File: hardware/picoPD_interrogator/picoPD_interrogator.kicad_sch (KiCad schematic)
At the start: 53 parts, among them J1 Conn_01x07, J2 USB_C_Receptacle_USB2.0_16P, J3 Conn_01x14, Q1 rohm-RE1C002UN, Q2 rohm-RE1C002UN, Q3 rohm-RE1C002UN, Q4 rohm-RE1C002UN, Q5 rohm-RE1C002UN, SW1 RESET_BTN, U3 ST-LM393QT, U6 LV2862XDDC

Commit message: PCB: Working on PCB layout.
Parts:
- TP1: footprint TestPoint:TestPoint_Pad_D4.0mm -> TestPoint:TestPoint_Pad_D2.5mm
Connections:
- net USB_DM_CONN: now reaches J2.A7 (D-), J2.B7 (D-), R27.2
- net USB_DP_CONN: now reaches J2.A6 (D+), J2.B6 (D+), R28.2
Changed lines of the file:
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@@
 		)
 	)
+	(label "USB_DP_CONN"
+		(at 264.16 57.15 180)
+		(effects
+			(font
+				(size 1.27 1.27)
+			)
+			(justify right)
+		)
+	)
 	(label "CC2_TX_L"
 		(at 133.35 63.5 180)
@@
 		)
 	)
+	(label "USB_DM_CONN"
+		(at 264.16 52.07 180)
+		(effects
+			(font
+				(size 1.27 1.27)
+			)
+			(justify right)
+		)
+	)
 	(label "SCL"
 		(at 36.83 99.06 0)
@@
 			)
 		)
-		(property "Footprint" "TestPoint:TestPoint_Pad_D4.0mm"
+		(property "Footprint" "TestPoint:TestPoint_Pad_D2.5mm"
 			(at 156.21 179.07 0)
 			(effects

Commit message: PCB: Working on board layout.
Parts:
- added R29: 3.3K, Resistor_SMD:R_0201_0603Metric, symbol Device:R
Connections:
- net 3V3: now also R29.2
- net TCPC_INT: now also R29.1
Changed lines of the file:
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@@
+	(wire
+		(pts
+			(xy 27.94 187.96) (xy 27.94 185.42)
+		)
+		(stroke
+			(width 0)
+			(type default)
+		)
+	)
 	(wire
 		(pts
@@
 	(wire
 		(pts
+			(xy 25.4 187.96) (xy 27.94 187.96)
+		)
+		(stroke
+			(width 0)
+			(type default)
+		)
+	)
+	(wire
+		(pts
+			(xy 27.94 177.8) (xy 27.94 175.26)
+		)
+		(stroke
+			(width 0)
+			(type default)
+		)
+	)
+	(wire
+		(pts
 			(xy 34.29 128.27) (xy 33.02 128.27)
 		)
@@
 		(pts
 			(xy 264.16 111.76) (xy 270.51 111.76)
+		)
+		(stroke
+			(width 0)
+			(type default)
+		)
+	)
+	(wire
+		(pts
+			(xy 27.94 175.26) (xy 35.56 175.26)
 		)
 		(stroke
@@
 	)
 	(label "TCPC_INT"
-		(at 35.56 175.26 180)
+		(at 33.02 175.26 180)
 		(effects
 			(font
@@
 			)
 			(justify left)
+		)
+	)
+	(label "3V3"
+		(at 25.4 187.96 180)
+		(effects
+			(font
+				(size 1.27 1.27)
+			)
+			(justify right)
 		)
 	)
@@
 					(unit 1)
 				)
+			)
+		)
+	)
+	(symbol
+		(lib_id "Device:R")
+		(at 27.94 181.61 0)
+		(unit 1)
+		(exclude_from_sim no)
+		(in_bom yes)
+		(on_board yes)
+		(dnp no)
+		(property "Reference" "R29"
+			(at 25.908 181.61 90)
+			(effects
+				(font
+					(size 1.27 1.27)
+				)
+			)
+		)
+		(property "Value" "3.3K"
+			(at 27.94 181.61 90)
+			(effects
+				(font
+					(size 0.889 0.889)
+				)
+			)
+		)
+		(property "Footprint" "Resistor_SMD:R_0201_0603Metric"
+			(at 26.162 181.61 90)
+			(effects
+				(font
+					(size 1.27 1.27)
+				)
+				(hide yes)
+			)
+		)
+		(property "Datasheet" "~"
+			(at 27.94 181.61 0)
+			(effects
+				(font
+					(size 1.27 1.27)
+				)
+				(hide yes)
+			)
+		)
+		(property "Description" "Resistor"
+			(at 27.94 181.61 0)
+			(effects
+				(font
+					(size 1.27 1.27)
+				)
+				(hide yes)
+			)
+		)
+		(property "Manufacturer" "Panasonic Electronic Components"
+			(at 27.94 181.61 0)
+			(effects
+				(font
+					(size 1.27 1.27)
+				)
+				(hide yes)
+			)
+		)
+		(property "Description Detailed" "3.3 kOhms ±1% 0.05W, 1/20W Chip Resistor 0201 (0603 Metric) Thick Film"
+			(at 27.94 181.61 0)
+			(effects
+				(font
+					(size 1.27 1.27)
+				)
+				(hide yes)
+			)
+		)
+		(property "DigiKey PN" "P122937CT-ND"
+			(at 27.94 181.61 0)
+			(effects
+				(font
+					(size 1.27 1.27)
+				)
+				(hide yes)
+			)
+		)
+		(property "Manufacturer PN" "ERJ-1GNF3301C"
+			(at 27.94 181.61 0)
+			(effects
+				(font
+					(size 1.27 1.27)
+				)
+				(hide yes)
+			)
+		)
+		(pin "1"
+		)
+		(pin "2"
+		)
+		(instances
+			(project "picoPD_interrogator"
+				(path "/e34b0978-7def-4921-94d0-accc0a677529"
+					(reference "R29")
+					(unit 1)
+				)

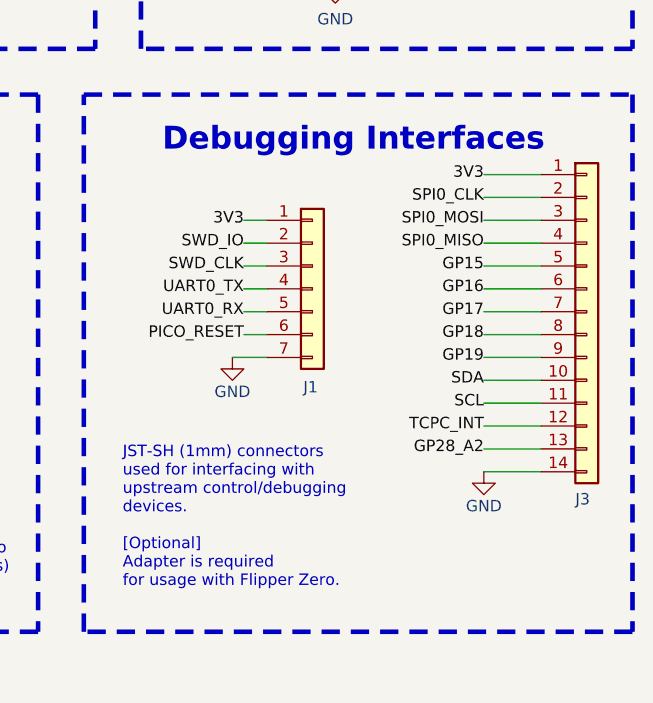
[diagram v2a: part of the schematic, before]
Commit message: PCB/Schematic: Added JST connector pins to the GND netlist.
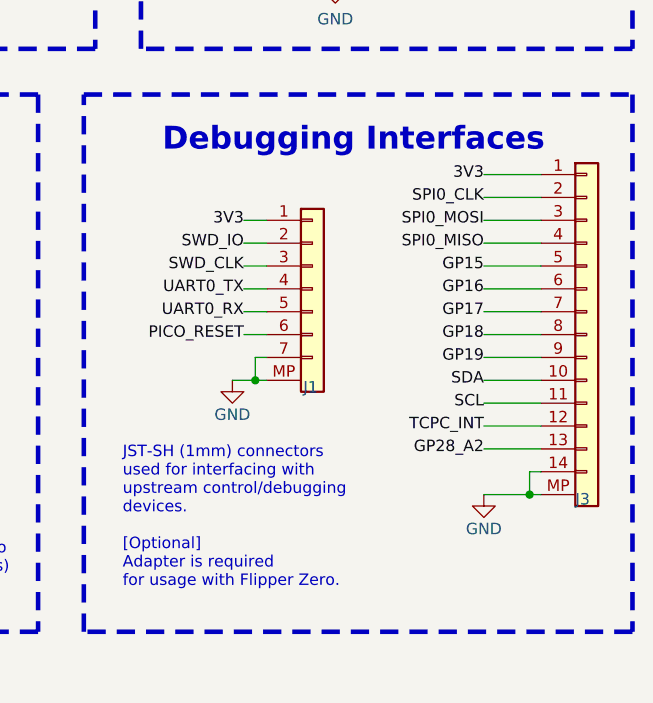
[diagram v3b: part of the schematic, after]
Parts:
- J1: symbol Connector_Generic:Conn_01x07 -> picoPD_interrogator:JST_7_pin
- J3: symbol Connector_Generic:Conn_01x14 -> picoPD_interrogator:JST_14_pin
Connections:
- net GND: now also J1.MP, J3.MP
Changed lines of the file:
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@@
 	)
 	(junction
+		(at 238.76 119.38)
+		(diameter 0)
+		(color 0 0 0 0)
+	)
+	(junction
 		(at 204.47 43.18)
 		(diameter 0)
@@
 	)
 	(junction
+		(at 269.24 132.08)
+		(diameter 0)
+		(color 0 0 0 0)
+	)
+	(junction
 		(at 143.51 116.84)
 		(diameter 0)
@@
 	(wire
 		(pts
-			(xy 264.16 129.54) (xy 270.51 129.54)
+			(xy 113.03 54.61) (xy 113.03 55.88)
 		)
 		(stroke
@@
 	(wire
 		(pts
-			(xy 113.03 54.61) (xy 113.03 55.88)
+			(xy 170.18 53.34) (xy 170.18 64.77)
 		)
 		(stroke
@@
 	(wire
 		(pts
-			(xy 170.18 53.34) (xy 170.18 64.77)
+			(xy 264.16 132.08) (xy 269.24 132.08)
 		)
 		(stroke
@@
 	(wire
 		(pts
-			(xy 236.22 116.84) (xy 240.03 116.84)
+			(xy 236.22 119.38) (xy 238.76 119.38)
 		)
 		(stroke
@@
 	(wire
 		(pts
+			(xy 240.03 116.84) (xy 238.76 116.84)
+		)
+		(stroke
+			(width 0)
+			(type default)
+		)
+	)
+	(wire
+		(pts
 			(xy 25.4 187.96) (xy 27.94 187.96)
 		)
@@
 	(wire
 		(pts
+			(xy 269.24 129.54) (xy 269.24 132.08)
+		)
+		(stroke
+			(width 0)
+			(type default)
+		)
+	)
+	(wire
+		(pts
 			(xy 95.25 116.84) (xy 95.25 118.11)
 		)
@@
 	(wire
 		(pts
+			(xy 238.76 119.38) (xy 240.03 119.38)
+		)
+		(stroke
+			(width 0)
+			(type default)
+		)
+	)
+	(wire
+		(pts
 			(xy 123.19 167.64) (xy 116.84 167.64)
 		)
@@
 	(wire
 		(pts
+			(xy 270.51 129.54) (xy 269.24 129.54)
+		)
+		(stroke
+			(width 0)
+			(type default)
+		)
+	)
+	(wire
+		(pts
 			(xy 203.2 55.88) (xy 203.2 59.69)
 		)
@@
 	(wire
 		(pts
+			(xy 238.76 116.84) (xy 238.76 119.38)
+		)
+		(stroke
+			(width 0)
+			(type default)
+		)
+	)
+	(wire
+		(pts
 			(xy 204.47 59.69) (xy 204.47 63.5)
 		)
@@
 	(wire
 		(pts
+			(xy 269.24 132.08) (xy 270.51 132.08)
+		)
+		(stroke
+			(width 0)
+			(type default)
+		)
+	)
+	(wire
+		(pts
 			(xy 91.44 106.68) (xy 95.25 106.68)
 		)
@@
 	(symbol
 		(lib_id "power:GND")
-		(at 236.22 116.84 0)
+		(at 236.22 119.38 0)
 		(unit 1)
 		(exclude_from_sim no)
@@
 		(dnp no)
 		(property "Reference" "#PWR023"
-			(at 236.22 123.19 0)
+			(at 236.22 125.73 0)
 			(effects
 				(font
@@
 		)
 		(property "Value" "GND"
-			(at 236.22 120.65 0)
+			(at 236.22 123.19 0)
 			(effects
 				(font
@@
 		)
 		(property "Footprint" ""
-			(at 236.22 116.84 0)
+			(at 236.22 119.38 0)
 			(effects
 				(font
@@
 		)
 		(property "Datasheet" ""
-			(at 236.22 116.84 0)
+			(at 236.22 119.38 0)
 			(effects
 				(font
@@
 		)
 		(property "Description" "Power symbol creates a global label with name \"GND\" , ground"
-			(at 236.22 116.84 0)
+			(at 236.22 119.38 0)
 			(effects
 				(font
@@
 	(symbol
 		(lib_id "power:GND")
-		(at 264.16 129.54 0)
+		(at 264.16 132.08 0)
 		(unit 1)
 		(exclude_from_sim no)
@@
 		(dnp no)
 		(property "Reference" "#PWR025"
-			(at 264.16 135.89 0)
+			(at 264.16 138.43 0)
 			(effects
 				(font
@@
 		)
 		(property "Value" "GND"
-			(at 264.16 133.35 0)
+			(at 264.16 135.89 0)
 			(effects
 				(font
@@
 		)
 		(property "Footprint" ""
-			(at 264.16 129.54 0)
+			(at 264.16 132.08 0)
 			(effects
 				(font
@@
 		)
 		(property "Datasheet" ""
-			(at 264.16 129.54 0)
+			(at 264.16 132.08 0)
 			(effects
 				(font
@@
 		)
 		(property "Description" "Power symbol creates a global label with name \"GND\" , ground"
-			(at 264.16 129.54 0)
+			(at 264.16 132.08 0)
 			(effects
 				(font
@@
 	)
 	(symbol
-		(lib_id "Connector_Generic:Conn_01x07")
+		(lib_id "picoPD_interrogator:JST_7_pin")
 		(at 245.11 109.22 0)
 		(unit 1)
@@
 		(pin "5"
 		)
+		(pin "MP"
+		)
 		(instances
 			(project ""
@@
 	)
 	(symbol
-		(lib_id "Connector_Generic:Conn_01x14")
+		(lib_id "picoPD_interrogator:JST_14_pin")
 		(at 275.59 111.76 0)
 		(unit 1)
@@
 		(pin "8"
 		)
+		(pin "MP"
+		)
 		(instances

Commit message: PCB: Working on PCB layout.
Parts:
- added C7: 1uF, Capacitor_SMD:C_0603_1608Metric, symbol Device:C
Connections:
- net 3V3: now also C7.2
- net GND: now also C7.1
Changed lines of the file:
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@@
 	)
 	(junction
+		(at 62.23 180.34)
+		(diameter 0)
+		(color 0 0 0 0)
+	)
+	(junction
 		(at 114.3 184.15)
 		(diameter 0)
@@
 	)
 	(junction
+		(at 57.15 172.72)
+		(diameter 0)
+		(color 0 0 0 0)
+	)
+	(junction
 		(at 143.51 116.84)
 		(diameter 0)
@@
 	)
 	(junction
-		(at 57.15 175.26)
+		(at 62.23 172.72)
 		(diameter 0)
 		(color 0 0 0 0)
@@
 	(wire
 		(pts
+			(xy 62.23 172.72) (xy 63.5 172.72)
+		)
+		(stroke
+			(width 0)
+			(type default)
+		)
+	)
+	(wire
+		(pts
 			(xy 102.87 54.61) (xy 102.87 55.88)
 		)
@@
 	(wire
 		(pts
+			(xy 57.15 172.72) (xy 62.23 172.72)
+		)
+		(stroke
+			(width 0)
+			(type default)
+		)
+	)
+	(wire
+		(pts
 			(xy 237.49 106.68) (xy 240.03 106.68)
 		)
@@
 	(wire
 		(pts
-			(xy 57.15 175.26) (xy 58.42 175.26)
-		)
-		(stroke
-			(width 0)
-			(type default)
-		)
-	)
-	(wire
-		(pts
 			(xy 63.5 78.74) (xy 66.04 78.74)
 		)
@@
 	(wire
 		(pts
-			(xy 57.15 172.72) (xy 57.15 175.26)
-		)
-		(stroke
-			(width 0)
-			(type default)
-		)
-	)
-	(wire
-		(pts
 			(xy 102.87 55.88) (xy 102.87 57.15)
 		)
@@
 	(wire
 		(pts
-			(xy 55.88 180.34) (xy 58.42 180.34)
+			(xy 55.88 180.34) (xy 62.23 180.34)
 		)
 		(stroke
@@
 	(wire
 		(pts
-			(xy 58.42 180.34) (xy 58.42 181.61)
-		)
-		(stroke
-			(width 0)
-			(type default)
-		)
-	)
-	(wire
-		(pts
 			(xy 170.18 39.37) (xy 170.18 53.34)
 		)
@@
 	(wire
 		(pts
+			(xy 57.15 172.72) (xy 57.15 175.26)
+		)
+		(stroke
+			(width 0)
+			(type default)
+		)
+	)
+	(wire
+		(pts
+			(xy 62.23 180.34) (xy 62.23 181.61)
+		)
+		(stroke
+			(width 0)
+			(type default)
+		)
+	)
+	(wire
+		(pts
 			(xy 269.24 132.08) (xy 270.51 132.08)
 		)
@@
 	)
 	(label "3V3"
-		(at 58.42 175.26 0)
+		(at 63.5 172.72 0)
 		(effects
 			(font
@@
 	(symbol
 		(lib_id "power:GND")
-		(at 58.42 181.61 0)
+		(at 62.23 181.61 0)
 		(mirror y)
 		(unit 1)
@@
 		(dnp no)
 		(property "Reference" "#PWR06"
-			(at 58.42 187.96 0)
+			(at 62.23 187.96 0)
 			(effects
 				(font
@@
 		)
 		(property "Value" "GND"
-			(at 62.738 183.134 0)
+			(at 66.548 183.134 0)
 			(effects
 				(font
@@
 		)
 		(property "Footprint" ""
-			(at 58.42 181.61 0)
+			(at 62.23 181.61 0)
 			(effects
 				(font
@@
 		)
 		(property "Datasheet" ""
-			(at 58.42 181.61 0)
+			(at 62.23 181.61 0)
 			(effects
 				(font
@@
 		)
 		(property "Description" "Power symbol creates a global label with name \"GND\" , ground"
-			(at 58.42 181.61 0)
+			(at 62.23 181.61 0)
 			(effects
 				(font
@@
 					(unit 1)
 				)
+			)
+		)
+	)
+	(symbol
+		(lib_id "Device:C")
+		(at 62.23 176.53 180)
+		(unit 1)
+		(exclude_from_sim no)
+		(in_bom yes)
+		(on_board yes)
+		(dnp no)
+		(property "Reference" "C7"
+			(at 65.532 174.244 0)
+			(effects
+				(font
+					(size 1.27 1.27)
+				)
+				(justify left)
+			)
+		)
+		(property "Value" "1uF"
+			(at 66.294 179.07 0)
+			(effects
+				(font
+					(size 1.27 1.27)
+				)
+				(justify left)
+			)
+		)
+		(property "Footprint" "Capacitor_SMD:C_0603_1608Metric"
+			(at 61.2648 172.72 0)
+			(effects
+				(font
+					(size 1.27 1.27)
+				)
+				(hide yes)
+			)
+		)
+		(property "Datasheet" "~"
+			(at 62.23 176.53 0)
+			(effects
+				(font
+					(size 1.27 1.27)
+				)
+				(hide yes)
+			)
+		)
+		(property "Description" "Unpolarized capacitor"
+			(at 62.23 176.53 0)
+			(effects
+				(font
+					(size 1.27 1.27)
+				)
+				(hide yes)
+			)
+		)
+		(property "Description Detailed" "1 µF ±10% 50V Ceramic Capacitor X5R 0603 (1608 Metric)"
+			(at 62.23 176.53 0)
+			(effects
+				(font
+					(size 1.27 1.27)
+				)
+				(hide yes)
+			)
+		)
+		(property "Manufacturer PN" "GRT188R61H105KE13D"
+			(at 62.23 176.53 0)
+			(effects
+				(font
+					(size 1.27 1.27)
+				)
+				(hide yes)
+			)
+		)
+		(property "Manufacturer" "Murata Electronics"
+			(at 62.23 176.53 0)
+			(effects
+				(font
+					(size 1.27 1.27)
+				)
+				(hide yes)
+			)
+		)
+		(property "DigiKey PN" "490-12330-1-ND"
+			(at 62.23 176.53 0)
+			(effects
+				(font
+					(size 1.27 1.27)
+				)
+				(hide yes)
+			)
+		)
+		(pin "2"
+		)
+		(pin "1"
+		)
+		(instances
+			(project "picoPD_interrogator"
+				(path "/e34b0978-7def-4921-94d0-accc0a677529"
+					(reference "C7")
+					(unit 1)
+				)

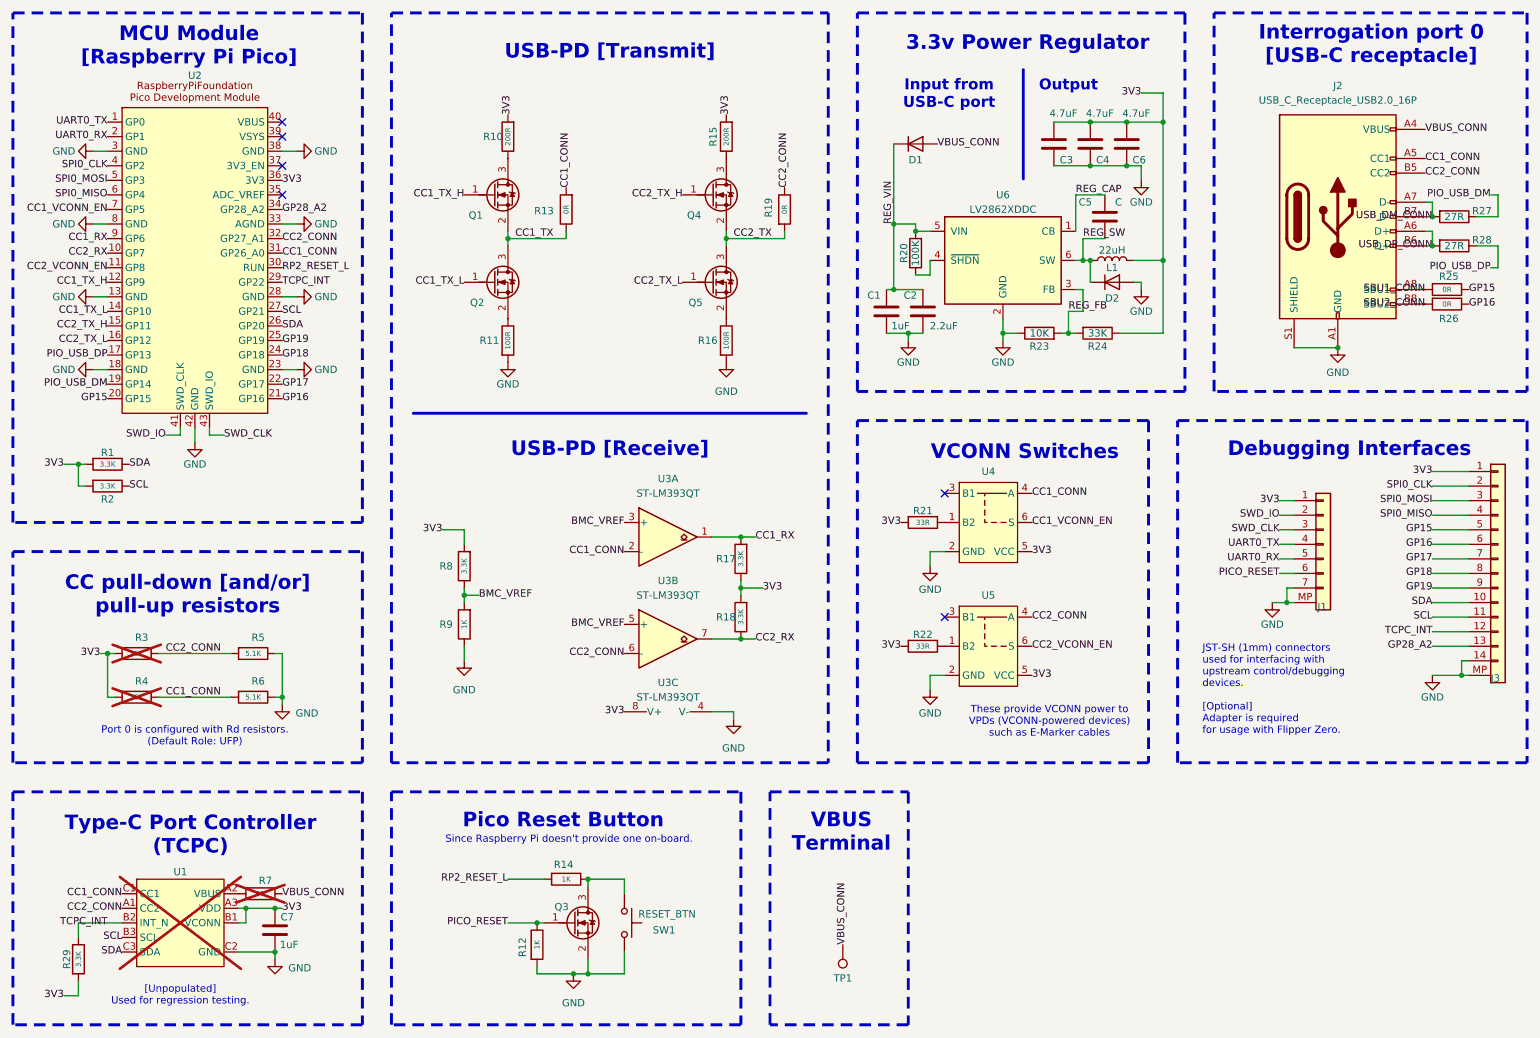
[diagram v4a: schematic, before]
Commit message: PCB/Schematic: Changed TCPC to FUSB302. (Unable to realistically route traces for TUSB422.)
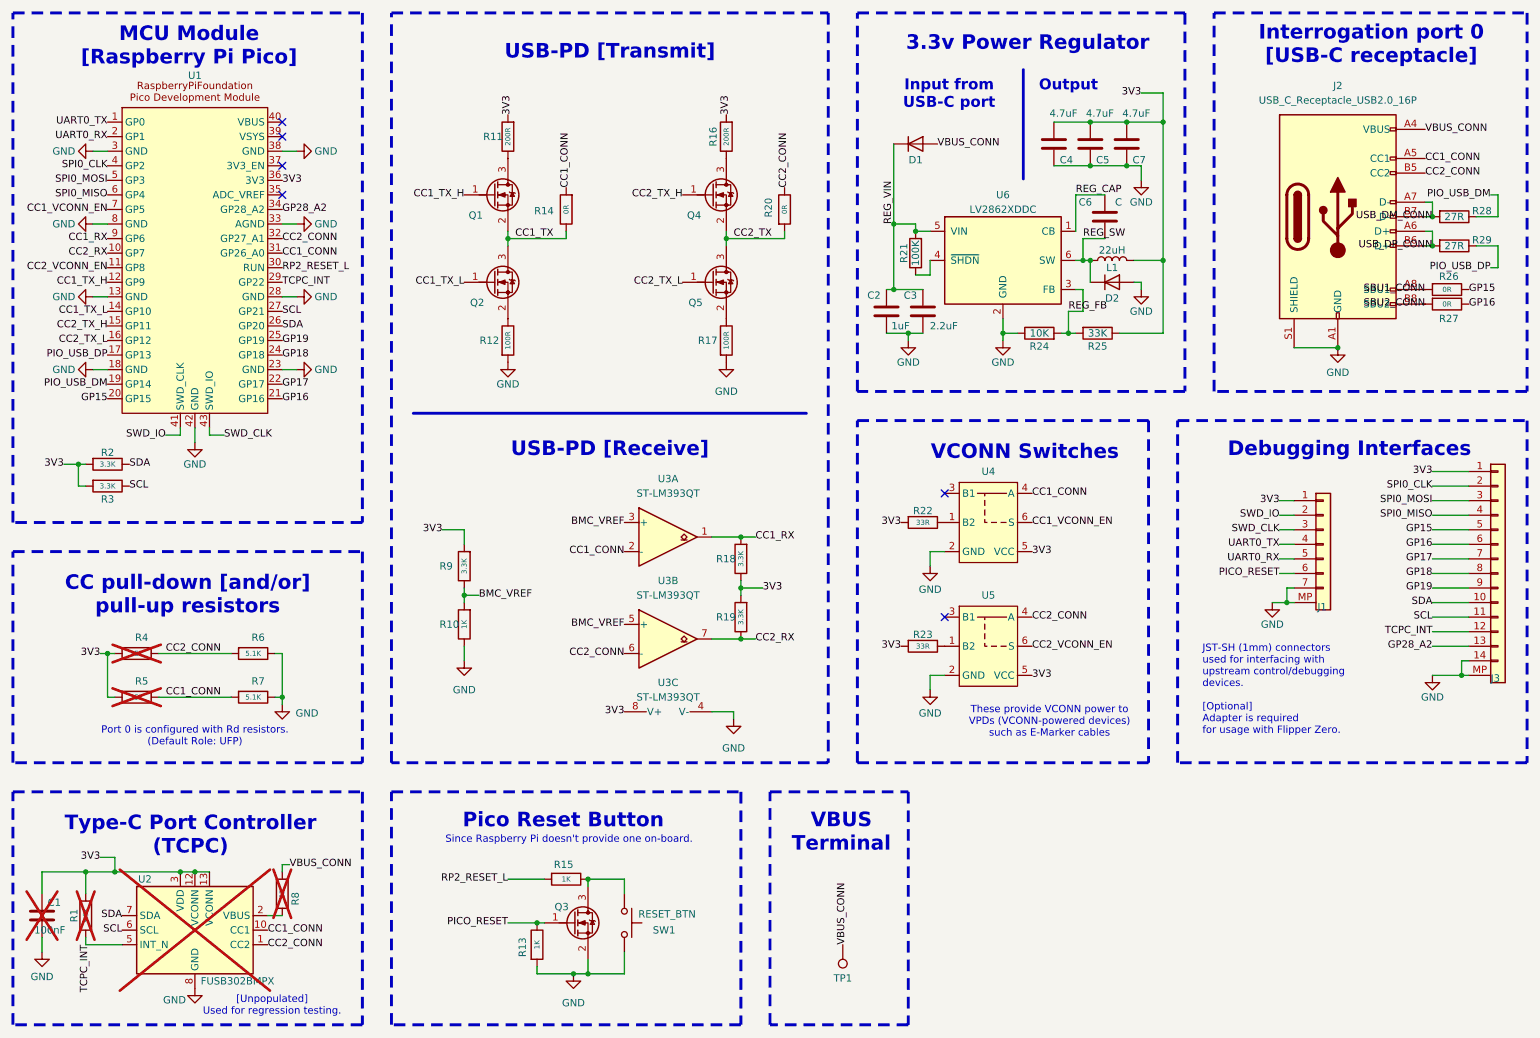
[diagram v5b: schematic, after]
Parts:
- removed C7: 1uF, Capacitor_SMD:C_0603_1608Metric, symbol Device:C
- removed R29: 3.3K, Resistor_SMD:R_0201_0603Metric, symbol Device:R
- removed R7: 0R, Resistor_SMD:R_0201_0603Metric, symbol Device:R
- removed U1: ~, picoPD_interrogator:WLCSP9_P0.4, symbol picoPD_interrogator:TCPC_WLCSP9
- added C1: 100nF, Capacitor_SMD:C_0201_0603Metric, symbol Device:C
- added R1: 3.3K, Resistor_SMD:R_0201_0603Metric, symbol Device:R
- added R8: 0R, Resistor_SMD:R_0201_0603Metric, symbol Device:R
- added U2: FUSB302BMPX, Package_DFN_QFN:WQFN-14-1EP_2.5x2.5mm_P0.5mm_EP1.45x1.45mm, symbol Interface_USB:FUSB302BMPX
- renumbered C1 to C2, C2 to C3, C3 to C4, C4 to C5, C5 to C6, C6 to C7, R9 to R10, R10 to R11, R11 to R12, R12 to R13, R13 to R14, R14 to R15, R15 to R16, R16 to R17, R17 to R18, R18 to R19, R1 to R2, R19 to R20, R20 to R21, R21 to R22, R22 to R23, R23 to R24, R24 to R25, R25 to R26, R26 to R27, R27 to R28, R28 to R29, R2 to R3, R3 to R4, R4 to R5, R5 to R6, R6 to R7, R8 to R9, U2 to U1
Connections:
- net 3V3: now also C1.2, R1.1, U2.12 (VCONN), U2.13 (VCONN), U2.3 (VDD), U2.4 (VDD)
- net CC1_CONN: now also U2.10 (CC1), U2.11 (CC1)
- net CC2_CONN: now also U2.1 (CC2), U2.14 (CC2)
- net GND: now also C1.1, U2.15 (GND), U2.8 (GND), U2.9 (GND)
- net SCL: now also U2.6 (SCL)
- net SDA: now also U2.7 (SDA)
- net TCPC_INT: now also R1.2, U2.5 (INT_N)
- net VBUS_CONN: now also R8.2
- new net: R8.1, U2.2 (VBUS)

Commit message: Schematic: Adjusted schematic for export to PDF.
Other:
- title: (none) -> picoPD_interrogator
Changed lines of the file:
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@@
 	(generator_version "9.0")
 	(paper "A4")
+	(title_block
+		(title "picoPD_interrogator")
+		(date "2025-07-23")
+		(rev "D - RC1")
+		(comment 1 "Uses RP2 PIO feature for USB-PD enumeration and testing")
+	)
 	(rectangle
 		(start 163.83 87.63)

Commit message: Changed items shown on BOM. (Raspberry Pi Pico board has been removed from BOM since this will be added manually.)
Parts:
- TP1: now left out of the parts list
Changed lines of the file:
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@@
 		(unit 1)
 		(exclude_from_sim no)
-		(in_bom yes)
+		(in_bom no)
 		(on_board yes)
 		(dnp no)
